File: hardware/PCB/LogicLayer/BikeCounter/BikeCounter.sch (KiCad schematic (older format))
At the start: 20 parts, among them J1 PIR sensor connector (TWIG-4P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, J2 AUX, J3 Vbat, J4 AM2320, SW1 SW_DIP_x03, U1 DS3231M

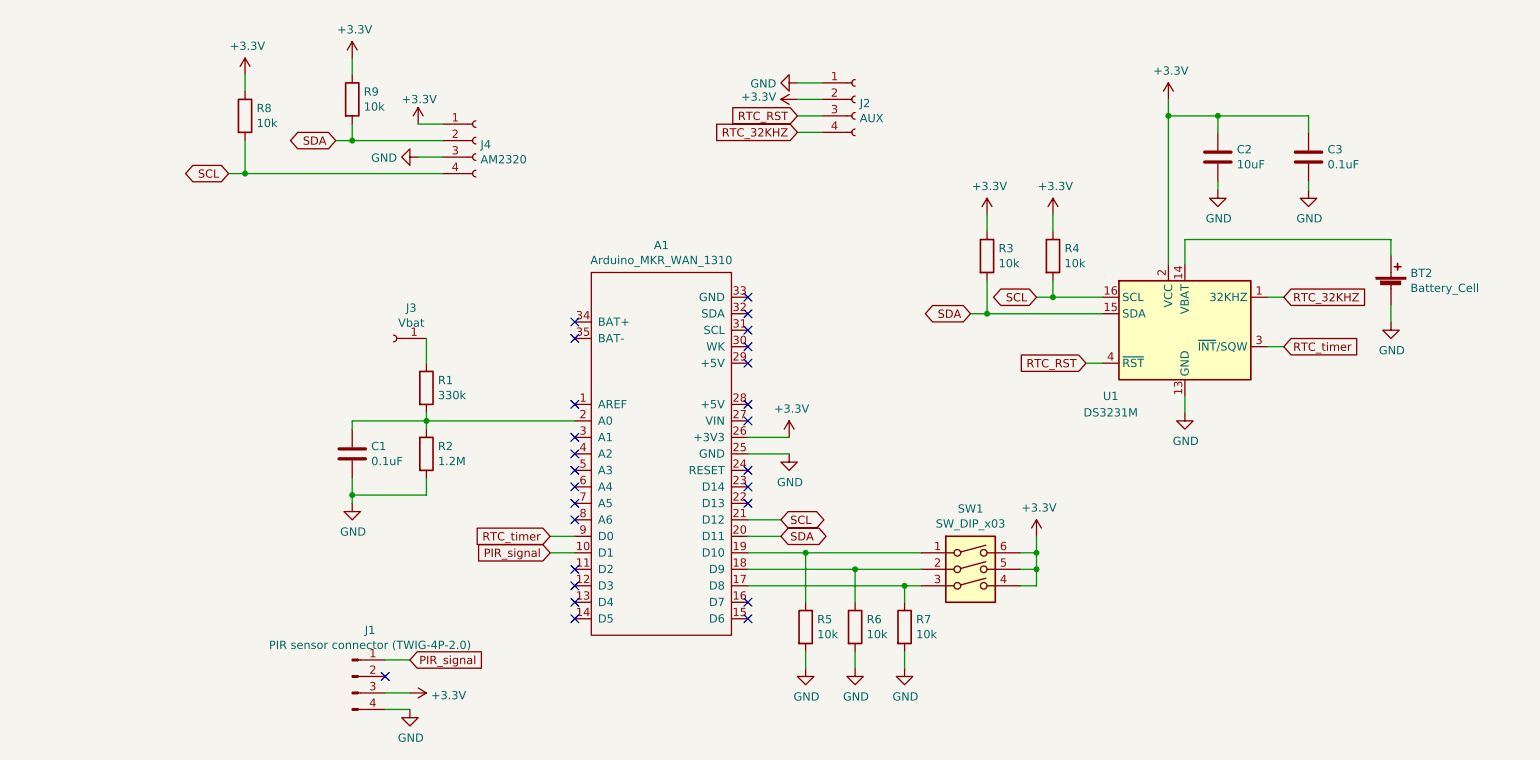
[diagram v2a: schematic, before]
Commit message: Final casing selected and PCB rearranged to fit into the casing
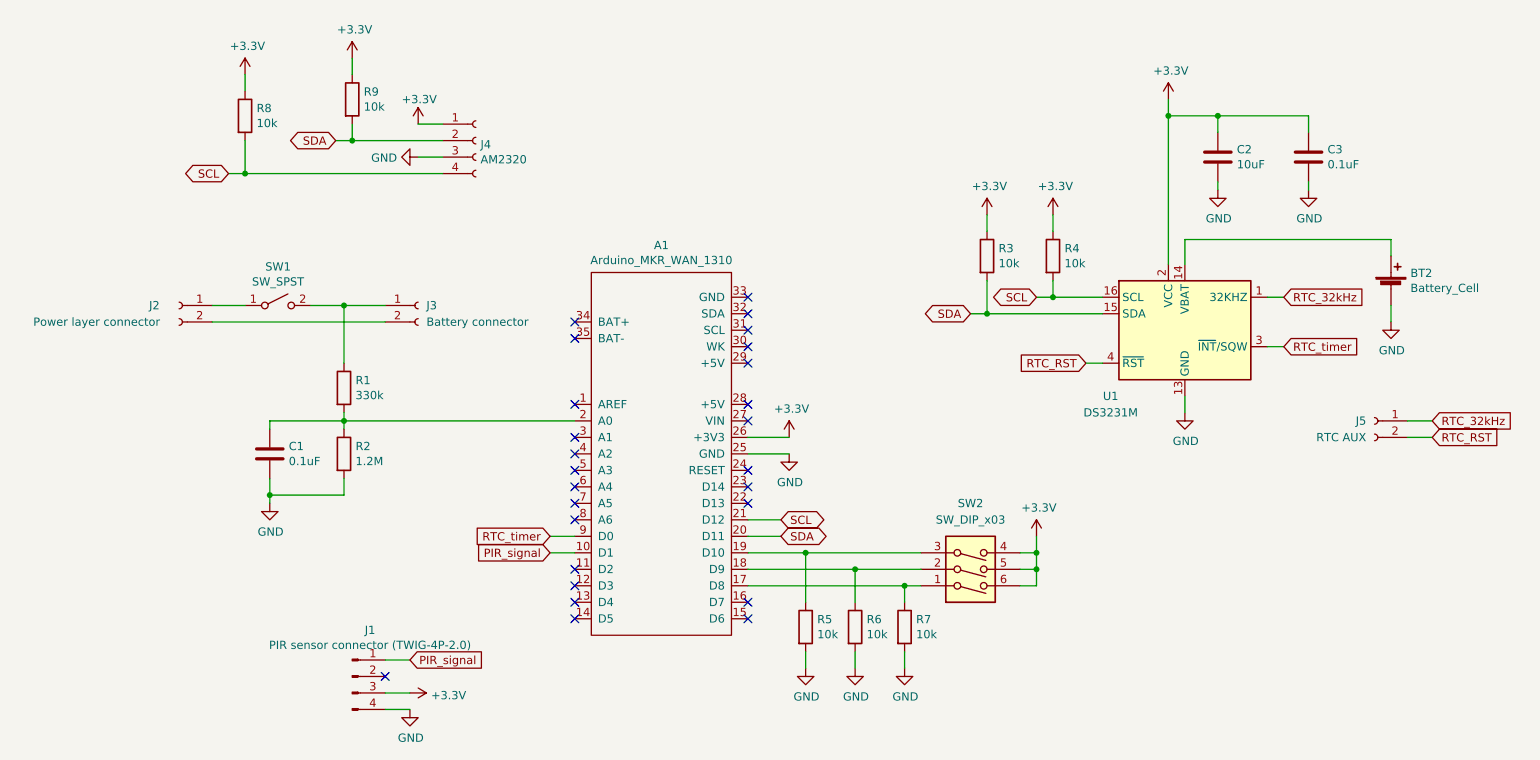
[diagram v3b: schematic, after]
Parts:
- removed J2: AUX, Connector_PinSocket_2.54mm:PinSocket_1x04_P2.54mm_Vertical, symbol Connector:Conn_01x04_Female
- removed J3: Vbat, Connector_PinSocket_2.54mm:PinSocket_1x01_P2.54mm_Vertical, symbol Connector:Conn_01x01_Female
- added J2: Power layer connector, Connector_PinSocket_2.54mm:PinSocket_1x02_P2.54mm_Vertical, symbol Connector:Conn_01x02_Female
- added J3: Battery connector, Connector_PinSocket_2.54mm:PinSocket_1x02_P2.54mm_Vertical, symbol Connector:Conn_01x02_Female
- added J5: RTC AUX, Connector_PinSocket_2.54mm:PinSocket_1x02_P2.54mm_Vertical, symbol Connector:Conn_01x02_Female
- added SW1: SW_SPST, General_TM:Switch_MHS12204, symbol Switch:SW_SPST
- renumbered SW1 to SW2
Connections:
- net RTC_RST: now also J5.2 (Pin_2)
- net at A1.17 (D8), R7.1: now also SW2.1; no longer SW2.3
- net at A1.19 (D10), R5.1: now also SW2.3; no longer SW2.1
- net at R1.1: now also J3.1 (Pin_1), SW1.2 (B)
- net RTC_32KHZ renamed RTC_32kHz
- net RTC_32kHz: now also J5.1 (Pin_1)
- new net: J2.2 (Pin_2), J3.2 (Pin_2)
- new net: J2.1 (Pin_1), SW1.1 (A)
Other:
- moved on the sheet: C1, R1, R2
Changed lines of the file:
@@
 L Device:R R2
 U 1 1 615B9C8E
-P 4050 3700
-F 0 "R2" H 4120 3746 50  0000 L CNN
-F 1 "1.2M" H 4120 3655 50  0000 L CNN
-F 2 "Resistor_SMD:R_1206_3216Metric_Pad1.42x1.75mm_HandSolder" V 3980 3700 50  0001 C CNN
-F 3 "~" H 4050 3700 50  0001 C CNN
-	1    4050 3700
+P 3550 3700
+F 0 "R2" H 3620 3746 50  0000 L CNN
+F 1 "1.2M" H 3620 3655 50  0000 L CNN
+F 2 "Resistor_SMD:R_1206_3216Metric_Pad1.42x1.75mm_HandSolder" V 3480 3700 50  0001 C CNN
+F 3 "~" H 3550 3700 50  0001 C CNN
+	1    3550 3700
 	1    0    0    -1
 $EndComp
@@
 L Device:R R1
 U 1 1 615BA347
-P 4050 3300
-F 0 "R1" H 4120 3346 50  0000 L CNN
-F 1 "330k" H 4120 3255 50  0000 L CNN
-F 2 "Resistor_SMD:R_1206_3216Metric_Pad1.42x1.75mm_HandSolder" V 3980 3300 50  0001 C CNN
-F 3 "~" H 4050 3300 50  0001 C CNN
-	1    4050 3300
+P 3550 3300
+F 0 "R1" H 3620 3346 50  0000 L CNN
+F 1 "330k" H 3620 3255 50  0000 L CNN
+F 2 "Resistor_SMD:R_1206_3216Metric_Pad1.42x1.75mm_HandSolder" V 3480 3300 50  0001 C CNN
+F 3 "~" H 3550 3300 50  0001 C CNN
+	1    3550 3300
 	1    0    0    -1
 $EndComp
@@
 L Device:C C1
 U 1 1 615B5D7E
-P 3600 3700
-F 0 "C1" H 3715 3746 50  0000 L CNN
-F 1 "0.1uF" H 3715 3655 50  0000 L CNN
-F 2 "Capacitor_SMD:C_0805_2012Metric_Pad1.15x1.40mm_HandSolder" H 3638 3550 50  0001 C CNN
-F 3 "~" H 3600 3700 50  0001 C CNN
-	1    3600 3700
-	1    0    0    -1
-$EndComp
-Wire Wire Line
-	4050 3450 4050 3500
-Wire Wire Line
-	3600 3550 3600 3500
-Wire Wire Line
-	3600 3500 4050 3500
-Connection ~ 4050 3500
-Wire Wire Line
-	4050 3500 4050 3550
-Wire Wire Line
-	4050 3950 4050 3850
-Wire Wire Line
-	4050 3950 3600 3950
-Wire Wire Line
-	3600 3950 3600 3850
+P 3100 3700
+F 0 "C1" H 3215 3746 50  0000 L CNN
+F 1 "0.1uF" H 3215 3655 50  0000 L CNN
+F 2 "Capacitor_SMD:C_0805_2012Metric_Pad1.15x1.40mm_HandSolder" H 3138 3550 50  0001 C CNN
+F 3 "~" H 3100 3700 50  0001 C CNN
+	1    3100 3700
+	1    0    0    -1
+$EndComp
+Wire Wire Line
+	3550 3450 3550 3500
+Wire Wire Line
+	3100 3550 3100 3500
+Wire Wire Line
+	3100 3500 3550 3500
+Connection ~ 3550 3500
+Wire Wire Line
+	3550 3500 3550 3550
+Wire Wire Line
+	3550 3950 3550 3850
+Wire Wire Line
+	3550 3950 3100 3950
+Wire Wire Line
+	3100 3950 3100 3850
 $Comp
 L power:GND #PWR0104
 U 1 1 615B913B
-P 3600 4000
-F 0 "#PWR0104" H 3600 3750 50  0001 C CNN
-F 1 "GND" H 3605 3827 50  0000 C CNN
-F 2 "" H 3600 4000 50  0001 C CNN
-F 3 "" H 3600 4000 50  0001 C CNN
-	1    3600 4000
-	1    0    0    -1
-$EndComp
-Wire Wire Line
-	3600 4000 3600 3950
-Connection ~ 3600 3950
-$Comp
-L Timer_RTC:DS3231M U1
-U 1 1 615C6A37
-P 8650 2950
-F 0 "U1" H 8200 2550 50  0000 C CNN
-F 1 "DS3231M" H 8200 2450 50  0000 C CNN
-F 2 "Package_SO:SOIC-16W_7.5x10.3mm_P1.27mm" H 8650 2350 50  0001 C CNN
-F 3 "http://datasheets.maximintegrated.com/en/ds/DS3231.pdf" H 8920 3000 50  0001 C CNN
-	1    8650 2950
-	1    0    0    -1
-$EndComp
+P 3100 4000
+F 0 "#PWR0104" H 3100 3750 50  0001 C CNN
+F 1 "GND" H 3105 3827 50  0000 C CNN
+F 2 "" H 3100 4000 50  0001 C CNN
+F 3 "" H 3100 4000 50  0001 C CNN
+	1    3100 4000
+	1    0    0    -1
+$EndComp
+Wire Wire Line
+	3100 4000 3100 3950
+Connection ~ 3100 3950
 $Comp
 L Device:R R4
@@
 Wire Wire Line
 	4800 4200 4950 4200
-Wire Wire Line
-	9150 3050 9250 3050
-$Comp
-L Connector:Conn_01x04_Female J2
-U 1 1 615E1037
-P 6650 1550
-F 0 "J2" H 6678 1526 50  0000 L CNN
-F 1 "AUX" H 6678 1435 50  0000 L CNN
-F 2 "Connector_PinSocket_2.54mm:PinSocket_1x04_P2.54mm_Vertical" H 6650 1550 50  0001 C CNN
-F 3 "~" H 6650 1550 50  0001 C CNN
-	1    6650 1550
-	1    0    0    -1
-$EndComp
-Wire Wire Line
-	8150 3150 8050 3150
-Wire Wire Line
-	9150 2750 9250 2750
-Wire Wire Line
-	6300 1650 6450 1650
-Wire Wire Line
-	6300 1750 6450 1750
 $Comp
 L Connector:Conn_01x04_Male J1
@@
 Wire Wire Line
 	4800 4300 4950 4300
-$Comp
-L power:GND #PWR0114
-U 1 1 615F4A01
-P 6300 1450
-F 0 "#PWR0114" H 6300 1200 50  0001 C CNN
-F 1 "GND" V 6305 1322 50  0000 R CNN
-F 2 "" H 6300 1450 50  0001 C CNN
-F 3 "" H 6300 1450 50  0001 C CNN
-	1    6300 1450
-	0    1    1    0
-$EndComp
-$Comp
-L power:+3.3V #PWR0115
-U 1 1 615F408E
-P 6300 1550
-F 0 "#PWR0115" H 6300 1400 50  0001 C CNN
-F 1 "+3.3V" V 6315 1678 50  0000 L CNN
-F 2 "" H 6300 1550 50  0001 C CNN
-F 3 "" H 6300 1550 50  0001 C CNN
-	1    6300 1550
-	0    -1   -1   0
-$EndComp
-Wire Wire Line
-	6450 1450 6300 1450
-Wire Wire Line
-	6450 1550 6300 1550
 Wire Wire Line
 	3800 4950 3950 4950
@@
 Text GLabel 4800 4200 0    50   Input ~ 0
 RTC_timer
-Text GLabel 9250 3050 2    50   Input ~ 0
-RTC_timer
-Text GLabel 9250 2750 2    50   Input ~ 0
-RTC_32KHZ
-Text GLabel 8050 3150 0    50   Input ~ 0
-RTC_RST
-Text GLabel 6300 1750 0    50   Input ~ 0
-RTC_32KHZ
-Text GLabel 6300 1650 0    50   Input ~ 0
-RTC_RST
 Wire Wire Line
 	9900 2500 9900 2400
@@
 	6000 4300 6350 4300
 $Comp
-L Switch:SW_DIP_x03 SW1
+L Switch:SW_DIP_x03 SW2
 U 1 1 61605D37
-P 7350 4500
-F 0 "SW1" H 7350 4967 50  0000 C CNN
-F 1 "SW_DIP_x03" H 7350 4876 50  0000 C CNN
-F 2 "Button_Switch_SMD:SW_DIP_SPSTx03_Slide_6.7x9.18mm_W8.61mm_P2.54mm_LowProfile" H 7350 4500 50  0001 C CNN
-F 3 "~" H 7350 4500 50  0001 C CNN
-	1    7350 4500
-	1    0    0    -1
+P 7350 4300
+F 0 "SW2" H 7350 4000 50  0000 C CNN
+F 1 "SW_DIP_x03" H 7350 4100 50  0000 C CNN
+F 2 "Button_Switch_SMD:SW_DIP_SPSTx03_Slide_6.7x9.18mm_W8.61mm_P2.54mm_LowProfile" H 7350 4300 50  0001 C CNN
+F 3 "~" H 7350 4300 50  0001 C CNN
+	1    7350 4300
+	1    0    0    1
 $EndComp
 NoConn ~ 4950 2900
 NoConn ~ 4950 3000
-$Comp
-L Connector:Conn_01x01_Female J3
-U 1 1 61A49201
-P 3850 3000
-F 0 "J3" H 3742 3185 50  0000 C CNN
-F 1 "Vbat" H 3742 3094 50  0000 C CNN
-F 2 "Connector_PinSocket_2.54mm:PinSocket_1x01_P2.54mm_Vertical" H 3850 3000 50  0001 C CNN
-F 3 "~" H 3850 3000 50  0001 C CNN
-	1    3850 3000
-	-1   0    0    -1
-$EndComp
-Wire Wire Line
-	4050 3000 4050 3150
-Wire Wire Line
-	4050 3500 4950 3500
 $Comp
 L Connector:Conn_01x04_Female J4
@@
 Wire Wire Line
 	3600 1800 4150 1800
+$Comp
+L Connector:Conn_01x02_Female J3
+U 1 1 61B73454
+P 4000 2800
+F 0 "J3" H 4050 2800 50  0000 L CNN
+F 1 "Battery connector" H 4050 2700 50  0000 L CNN
+F 2 "Connector_PinSocket_2.54mm:PinSocket_1x02_P2.54mm_Vertical" H 4000 2800 50  0001 C CNN
+F 3 "~" H 4000 2800 50  0001 C CNN
+	1    4000 2800
+	1    0    0    -1
+$EndComp
+Wire Wire Line
+	3550 3500 4950 3500
+$Comp
+L Connector:Conn_01x02_Female J2
+U 1 1 61B7F74F
+P 2550 2800
+F 0 "J2" H 2700 2800 50  0000 C CNN
+F 1 "Power layer connector" H 3050 2700 50  0000 C CNN
+F 2 "Connector_PinSocket_2.54mm:PinSocket_1x02_P2.54mm_Vertical" H 2550 2800 50  0001 C CNN
+F 3 "~" H 2550 2800 50  0001 C CNN
+	1    2550 2800
+	-1   0    0    -1
+$EndComp
+$Comp
+L Switch:SW_SPST SW1
+U 1 1 61B85A6B
+P 3150 2800
+F 0 "SW1" H 3150 3035 50  0000 C CNN
+F 1 "SW_SPST" H 3150 2944 50  0000 C CNN
+F 2 "General_TM:Switch_MHS12204" H 3150 2800 50  0001 C CNN
+F 3 "~" H 3150 2800 50  0001 C CNN
+	1    3150 2800
+	1    0    0    -1
+$EndComp
+Wire Wire Line
+	2750 2800 2950 2800
+Wire Wire Line
+	3350 2800 3550 2800
+Wire Wire Line
+	2750 2900 3800 2900
+Wire Wire Line
+	3550 2800 3550 3150
+Connection ~ 3550 2800
+Wire Wire Line
+	3550 2800 3800 2800
+$Comp
+L Timer_RTC:DS3231M U1
+U 1 1 615C6A37
+P 8650 2950
+F 0 "U1" H 8200 2550 50  0000 C CNN
+F 1 "DS3231M" H 8200 2450 50  0000 C CNN
+F 2 "Package_SO:SOIC-16W_7.5x10.3mm_P1.27mm" H 8650 2350 50  0001 C CNN
+F 3 "http://datasheets.maximintegrated.com/en/ds/DS3231.pdf" H 8920 3000 50  0001 C CNN
+	1    8650 2950
+	1    0    0    -1
+$EndComp
+Text GLabel 9250 3050 2    50   Input ~ 0
+RTC_timer
+Wire Wire Line
+	9150 3050 9250 3050
+Text GLabel 9250 2750 2    50   Input ~ 0
+RTC_32kHz
+Text GLabel 10150 3500 2    50   Input ~ 0
+RTC_32kHz
+Wire Wire Line
+	9150 2750 9250 2750
+Text GLabel 10150 3600 2    50   Input ~ 0
+RTC_RST
+Text GLabel 8050 3150 0    50   Input ~ 0
+RTC_RST
+Wire Wire Line
+	8050 3150 8150 3150
+$Comp
+L Connector:Conn_01x02_Female J5
+U 1 1 61BC8555
+P 9800 3500
+F 0 "J5" H 9850 3500 50  0000 L CNN
+F 1 "RTC AUX" H 9850 3400 50  0000 L CNN
+F 2 "Connector_PinSocket_2.54mm:PinSocket_1x02_P2.54mm_Vertical" H 9800 3500 50  0001 C CNN
+F 3 "~" H 9800 3500 50  0001 C CNN
+	1    9800 3500
+	-1   0    0    -1
+$EndComp
+Wire Wire Line
+	10000 3500 10150 3500
+Wire Wire Line
+	10000 3600 10150 3600
 $EndSCHEMATC
